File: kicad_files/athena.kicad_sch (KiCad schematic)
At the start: 557 parts, among them J1 TYPE-C-31-M12, J2 SM04B-SRSS-TB(LF)(SN), J3 SM04B-SRSS-TB(LF)(SN), Q1 2N7002, Q2 2N7002, Q3 AO3401A, Q4 2N7002, Q5 2N7002, SW1 K2-1187SQ-A4SW-06, SW10 MX Switch, SW100 MX Switch, SW101 MX Switch, SW102 MX Switch, SW103 MX Switch, SW104 MX Switch, SW105 MX Switch, SW106 MX Switch, SW107 MX Switch, SW108 MX Switch, SW109 MX Switch, SW11 MX Switch, SW110 MX Switch, SW111 MX Switch, SW112 MX Switch, SW113 MX Switch, SW12 MX Switch, SW13 MX Switch, SW14 MX Switch, SW15 MX Switch, SW16 MX Switch, SW17 MX Switch, SW18 MX Switch, SW19 MX Switch, SW2 MX Switch, SW20 MX Switch, SW21 MX Switch, SW22 MX Switch, SW23 MX Switch, SW24 MX Switch, SW25 MX Switch, SW26 MX Switch, SW27 MX Switch, SW28 MX Switch, SW29 MX Switch, SW3 MX Switch, SW30 MX Switch, SW31 MX Switch, SW32 MX Switch, SW33 MX Switch, SW34 MX Switch, SW35 MX Switch, SW36 MX Switch, SW37 MX Switch, SW38 MX Switch, SW39 MX Switch, SW4 MX Switch, SW40 MX Switch, SW41 MX Switch, SW42 MX Switch, SW43 MX Switch, SW44 MX Switch, SW45 MX Switch, SW46 MX Switch, SW47 MX Switch, SW48 MX Switch, SW49 MX Switch, SW5 MX Switch, SW50 MX Switch, SW51 MX Switch, SW52 MX Switch, SW53 MX Switch, SW54 MX Switch, SW55 MX Switch, SW56 MX Switch, SW57 MX Switch, SW58 MX Switch, SW59 MX Switch, SW6 MX Switch, SW60 MX Switch, SW61 MX Switch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

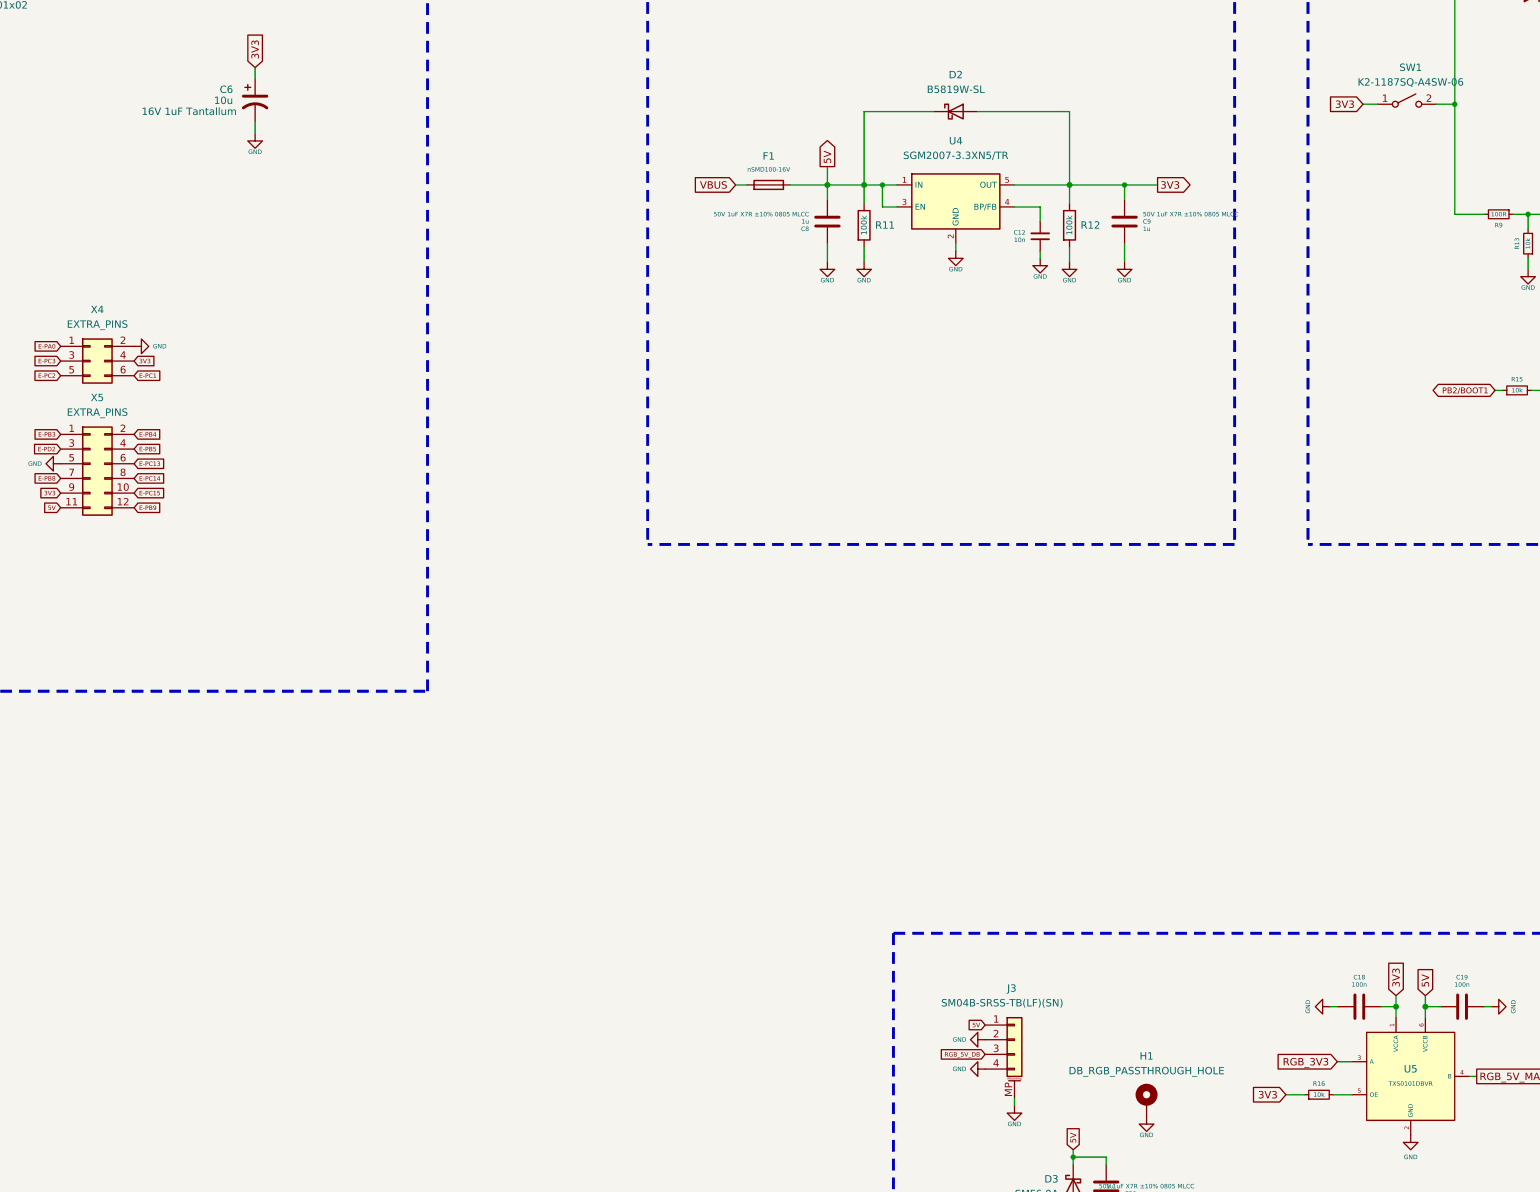
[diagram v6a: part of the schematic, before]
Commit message: RGB translator change
RGB translator changed from SC-70-6 version to SOT-563 due to JLC shortage of the former
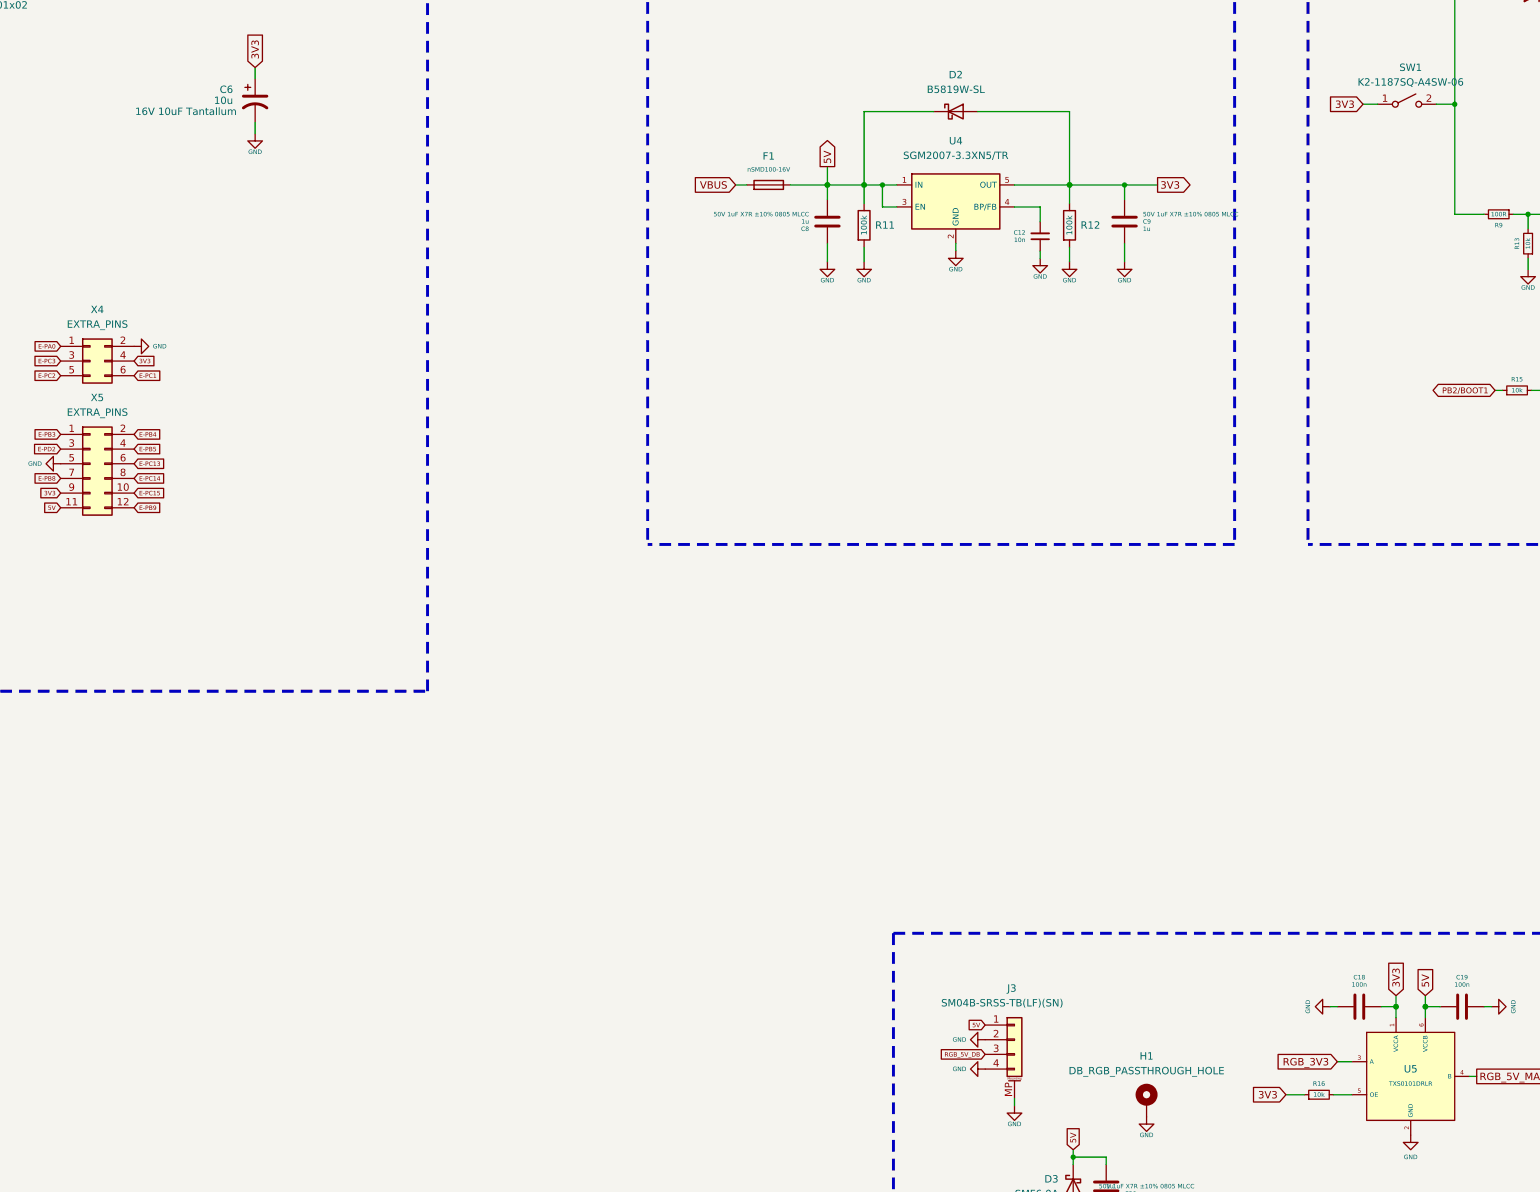
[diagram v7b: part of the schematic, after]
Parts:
- C6: Specification 16V 1uF Tantallum -> 16V 10uF Tantallum
- U5: value TXS0101DBVR -> TXS0101DRLR; footprint acheron_Components:SOT-23-6 -> acheron_Components:SOT-563; Manufacturer Part Number TXS0101DBVR -> TXS0101DRLR; Package SOT-23 -> SOT-563; Vendor Part Number LCSC C132604 -> LCSC C131928
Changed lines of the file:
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@@
   (title_block
     (title "Athena PCB schematic")
-    (date "2022-01-29")
-    (rev "V2.1.4")
+    (date "2022-02-04")
+    (rev "V2.1.5")
     (company "Acheron Project")
     (comment 1 "Designed by Gondolindrim")
@@
     (in_bom yes) (on_board yes)
     (property "Reference" "U5" (id 0) (at 601.98 262.255 0))
-    (property "Value" "TXS0101DBVR" (id 1) (at 601.98 264.795 0)
+    (property "Value" "TXS0101DRLR" (id 1) (at 601.98 264.795 0)
       (effects (font (size 0.762 0.762)))
     )
-    (property "Footprint" "acheron_Components:SOT-23-6" (id 2) (at 601.98 263.525 0)
+    (property "Footprint" "acheron_Components:SOT-563" (id 2) (at 601.98 263.525 0)
       (effects (font (size 1.27 1.27)) hide)
     )
@@
       (effects (font (size 1.27 1.27)) hide)
     )
-    (property "Manufacturer Part Number" "TXS0101DBVR" (id 5) (at 601.98 263.525 0)
+    (property "Manufacturer Part Number" "TXS0101DRLR" (id 5) (at 601.98 263.525 0)
       (effects (font (size 1.27 1.27)) hide)
     )
-    (property "LCSC Part Number" "" (id 6) (at 601.98 263.525 0)
+    (property "Package" "SOT-563" (id 7) (at 601.98 263.525 0)
       (effects (font (size 1.27 1.27)) hide)
     )
-    (property "Package" "SOT-23" (id 7) (at 601.98 263.525 0)
+    (property "Specification" "1-bit bidirectional logic voltage level translator" (id 8) (at 602.0054 263.525 0)
       (effects (font (size 1.27 1.27)) hide)
     )
-    (property "Specification" "1-bit bidirectional logic voltage level translator" (id 8) (at 601.98 263.525 0)
-      (effects (font (size 1.27 1.27)) hide)
-    )
-    (property "Vendor Part Number" "LCSC C132604" (id 10) (at 601.98 263.525 0)
+    (property "Vendor Part Number" "LCSC C131928" (id 10) (at 601.98 263.525 0)
       (effects (font (size 1.27 1.27)) hide)
     )
@@
       (effects (font (size 1.27 1.27)) hide)
     )
-    (property "Specification" "16V 1uF Tantallum" (id 5) (at 398.78 96.52 0)
+    (property "Specification" "16V 10uF Tantallum" (id 5) (at 398.78 96.52 0)
       (effects (font (size 1.27 1.27)) (justify right))
     )
@@
     )
     (path "/6f556440-bf01-4dc9-bfef-0ee4385d954a"
-      (reference "U5") (unit 1) (value "TXS0101DBVR") (footprint "acheron_Components:SOT-23-6")
+      (reference "U5") (unit 1) (value "TXS0101DRLR") (footprint "acheron_Components:SOT-563")
     )
     (path "/4013434a-d80b-495e-97c4-53e000bb1df9"

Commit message: Edit component metadata; prepare for release
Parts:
- X4, X5, X7: now left out of the parts list
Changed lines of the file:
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@@
   )
   (symbol (lib_id "Connector_Generic:Conn_02x03_Odd_Even") (at 373.38 139.7 0) (unit 1)
-    (in_bom yes) (on_board yes) (fields_autoplaced)
+    (in_bom no) (on_board yes) (fields_autoplaced)
     (property "Reference" "X4" (id 0) (at 374.65 130.81 0))
     (property "Value" "EXTRA_PINS" (id 1) (at 374.65 133.35 0))
@@
   )
   (symbol (lib_id "Connector_Generic:Conn_02x06_Odd_Even") (at 373.38 157.48 0) (unit 1)
-    (in_bom yes) (on_board yes)
+    (in_bom no) (on_board yes)
     (property "Reference" "X5" (id 0) (at 374.65 146.05 0))
     (property "Value" "EXTRA_PINS" (id 1) (at 374.65 148.59 0))
@@
   )
   (symbol (lib_id "Connector_Generic:Conn_01x03") (at 668.655 254 0) (unit 1)
-    (in_bom yes) (on_board yes)
+    (in_bom no) (on_board yes)
     (property "Reference" "X7" (id 0) (at 667.385 245.11 0)
       (effects (font (size 1.27 1.27)) (justify left))
@@
       (effects (font (size 1.27 1.27)) hide)
     )
-    (property "Specification" "" (id 7) (at 668.655 254 0)
-      (effects (font (size 1.27 1.27)) hide)
-    )
